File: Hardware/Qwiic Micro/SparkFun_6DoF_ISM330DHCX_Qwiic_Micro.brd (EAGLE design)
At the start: 19.1 x 7.6 mm, 42 parts, among them J1 Qwiic Right Angle, U1 ISM330DHCX

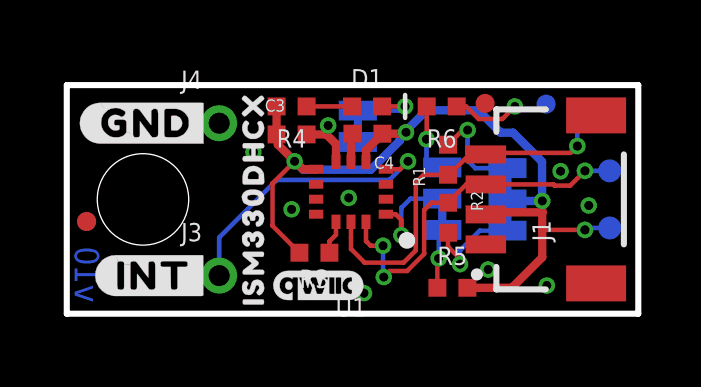
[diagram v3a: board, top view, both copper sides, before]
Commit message: Fixes silk for X-axis, changes tails on INT and GND silk
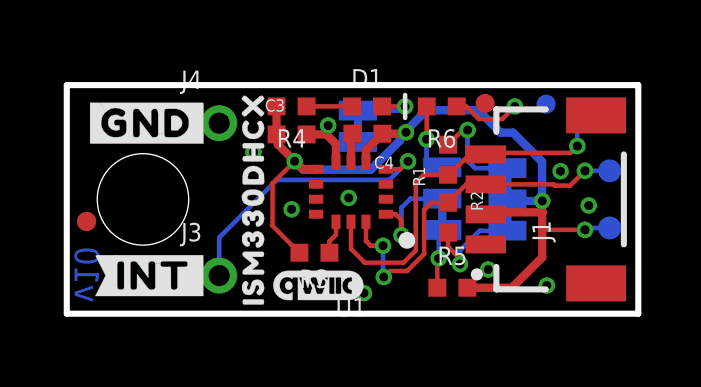
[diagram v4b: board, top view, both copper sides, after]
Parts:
- U$10: device top:#GND#2 -> top:#GND#4
- U$11: device top:#INT#3 -> top:#INT#21
- U$4: device top:#GND#0 -> top:#GND#4
- U$5: device top:#INT#1 -> top:#INT#20
- moved U$7 3.20 mm to (6.10, 1.65)
- moved U$8 3.05 mm to (9.27, 1.57)
- moved U$9 2.72 mm to (8.03, 5.00)
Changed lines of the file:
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@@
 <rectangle x1="9.1948" y1="4.953" x2="9.2456" y2="5.1816" layer="41"/>
 <dimension x1="2.54" y1="3.81" x2="0" y2="3.81" x3="1.27" y3="12.7" textsize="1.778" layer="47" dtype="horizontal" unit="inch"/>
-<wire x1="10.541" y1="3.305175" x2="8.636" y2="3.305175" width="0.254" layer="22"/>
-<wire x1="9.144" y1="2.797175" x2="9.144" y2="3.940175" width="0.254" layer="22" curve="180"/>
-<wire x1="9.144" y1="3.940175" x2="9.398" y2="4.067175" width="0.254" layer="22"/>
-<wire x1="9.144" y1="3.940175" x2="9.271" y2="3.686175" width="0.254" layer="22"/>
-<wire x1="10.541" y1="3.305175" x2="10.287" y2="3.051175" width="0.254" layer="22"/>
-<wire x1="10.541" y1="3.305175" x2="10.287" y2="3.559175" width="0.254" layer="22"/>
-<wire x1="7.635875" y1="0.65405" x2="7.635875" y2="2.43205" width="0.254" layer="22"/>
-<wire x1="7.000875" y1="2.05105" x2="8.270875" y2="2.05105" width="0.254" layer="22" curve="180"/>
-<wire x1="8.270875" y1="2.05105" x2="8.397875" y2="1.79705" width="0.254" layer="22"/>
-<wire x1="8.270875" y1="2.05105" x2="8.042275" y2="1.92405" width="0.254" layer="22"/>
-<wire x1="7.635875" y1="0.65405" x2="7.381875" y2="0.90805" width="0.254" layer="22"/>
-<wire x1="7.635875" y1="0.65405" x2="7.889875" y2="0.90805" width="0.254" layer="22"/>
-<wire x1="7.356475" y1="0.93345" x2="7.915275" y2="0.93345" width="0.254" layer="22"/>
-<wire x1="8.042275" y1="1.92405" x2="8.397875" y2="1.79705" width="0.254" layer="22"/>
-<wire x1="9.398" y1="4.067175" x2="9.271" y2="3.686175" width="0.254" layer="22"/>
-<wire x1="10.287" y1="3.559175" x2="10.287" y2="3.051175" width="0.254" layer="22"/>
-<wire x1="7.38505" y1="4.403725" x2="7.051675" y2="4.45135" width="0.254" layer="22"/>
-<wire x1="7.38505" y1="4.403725" x2="7.25805" y2="4.09575" width="0.254" layer="22"/>
-<wire x1="7.25805" y1="4.09575" x2="7.051675" y2="4.45135" width="0.254" layer="22"/>
-<wire x1="7.254875" y1="4.32435" x2="6.848475" y2="2.71145" width="0.254" layer="22" curve="100"/>
-<circle x="7.7089" y="3.35915" radius="0.5334" width="0.254" layer="22"/>
-<wire x1="8.128" y1="2.921" x2="7.239" y2="3.81" width="0.254" layer="22"/>
-<wire x1="7.366" y1="2.921" x2="8.255" y2="3.81" width="0.254" layer="22"/>
+<wire x1="5.207" y1="3.171825" x2="7.112" y2="3.171825" width="0.254" layer="22"/>
+<wire x1="6.604" y1="3.679825" x2="6.604" y2="2.536825" width="0.254" layer="22" curve="180"/>
+<wire x1="6.604" y1="2.536825" x2="6.35" y2="2.409825" width="0.254" layer="22"/>
+<wire x1="6.604" y1="2.536825" x2="6.477" y2="2.790825" width="0.254" layer="22"/>
+<wire x1="5.207" y1="3.171825" x2="5.461" y2="3.425825" width="0.254" layer="22"/>
+<wire x1="5.207" y1="3.171825" x2="5.461" y2="2.917825" width="0.254" layer="22"/>
+<wire x1="8.016875" y1="0.52705" x2="8.016875" y2="2.30505" width="0.254" layer="22"/>
+<wire x1="7.381875" y1="1.92405" x2="8.651875" y2="1.92405" width="0.254" layer="22" curve="180"/>
+<wire x1="8.651875" y1="1.92405" x2="8.778875" y2="1.67005" width="0.254" layer="22"/>
+<wire x1="8.651875" y1="1.92405" x2="8.423275" y2="1.79705" width="0.254" layer="22"/>
+<wire x1="8.016875" y1="0.52705" x2="7.762875" y2="0.78105" width="0.254" layer="22"/>
+<wire x1="8.016875" y1="0.52705" x2="8.270875" y2="0.78105" width="0.254" layer="22"/>
+<wire x1="7.737475" y1="0.80645" x2="8.296275" y2="0.80645" width="0.254" layer="22"/>
+<wire x1="8.423275" y1="1.79705" x2="8.778875" y2="1.67005" width="0.254" layer="22"/>
+<wire x1="6.35" y1="2.409825" x2="6.477" y2="2.790825" width="0.254" layer="22"/>
+<wire x1="5.461" y1="2.917825" x2="5.461" y2="3.425825" width="0.254" layer="22"/>
+<wire x1="9.229725" y1="3.53695" x2="9.27735" y2="3.870325" width="0.254" layer="22"/>
+<wire x1="9.229725" y1="3.53695" x2="8.92175" y2="3.66395" width="0.254" layer="22"/>
+<wire x1="8.92175" y1="3.66395" x2="9.27735" y2="3.870325" width="0.254" layer="22"/>
+<wire x1="9.15035" y1="3.667125" x2="7.53745" y2="4.073525" width="0.254" layer="22" curve="100"/>
+<circle x="8.0899" y="3.23215" radius="0.5334" width="0.254" layer="22"/>
+<wire x1="8.509" y1="2.794" x2="7.62" y2="3.683" width="0.254" layer="22"/>
+<wire x1="7.747" y1="2.794" x2="8.636" y2="3.683" width="0.254" layer="22"/>
 <dimension x1="19.05" y1="7.62" x2="0" y2="7.62" x3="9.525" y3="16.51" textsize="1.778" textratio="15" layer="47" unit="inch"/>
 <dimension x1="19.05" y1="0" x2="19.05" y2="7.62" x3="27.94" y3="3.81" textsize="1.778" textratio="15" layer="47" unit="inch"/>
@@
 <element name="LOGO1" library="SparkFun-Aesthetics" package="QWIIC_3MM" value="QWIIC_LOGO_3MM" x="8.382" y="0.9398" smashed="yes"/>
 <element name="LOGO3" library="SparkFun-Aesthetics" package="BLANK" value="SFE_LOGO_NAME_FLAMEBLANK" x="-39.37" y="-15.24" smashed="yes"/>
-<element name="U$7" library="ISMTopMini" package="X2114" value="" x="9.271" y="2.032" smashed="yes" rot="MR0"/>
-<element name="U$8" library="ISMTopMini" package="Y2115" value="" x="6.223" y="1.5748" smashed="yes" rot="MR0"/>
-<element name="U$9" library="ISMTopMini" package="Z2116" value="" x="5.8674" y="3.3528" smashed="yes" rot="MR0"/>
+<element name="U$7" library="ISMTopMini" package="X2114" value="" x="6.096" y="1.651" smashed="yes" rot="MR0"/>
+<element name="U$8" library="ISMTopMini" package="Y2115" value="" x="9.271" y="1.5748" smashed="yes" rot="MR0"/>
+<element name="U$9" library="ISMTopMini" package="Z2116" value="" x="8.0264" y="5.0038" smashed="yes" rot="MR0"/>
 <element name="U$3" library="ISMTopMini" package="#LED#2121" value="" x="7.3406" y="6.35" smashed="yes" rot="MR0"/>
 <element name="U$6" library="ISMTopMini" package="ISM330DHCX2120" value="" x="6.223" y="3.8354" smashed="yes" rot="R90"/>
@@
 </element>
 <element name="TP4" library="SparkFun-Connectors" package="PAD.03X.03" value="TEST-POINT3" x="18.0975" y="0.9525" smashed="yes" rot="MR0"/>
-<element name="U$4" library="top" package="#GND#0" value="" x="2.667" y="6.35" smashed="yes"/>
-<element name="U$5" library="top" package="#INT#1" value="" x="2.921" y="1.27" smashed="yes"/>
-<element name="U$10" library="top" package="#GND#2" value="" x="2.667" y="6.35" smashed="yes" rot="MR0"/>
-<element name="U$11" library="top" package="#INT#3" value="" x="2.921" y="1.27" smashed="yes" rot="MR0"/>
 <element name="U$1" library="top" package="#0#4" value="" x="12.573" y="6.35" smashed="yes" rot="MR90"/>
 <element name="U$2" library="top" package="#1#4" value="" x="12.446" y="1.397" smashed="yes" rot="MR90"/>
@@
 <attribute name="VALUE" x="8.255" y="2.594" size="0.6096" layer="27" font="vector" ratio="20" rot="R180" align="top-center"/>
 </element>
+<element name="U$5" library="top" package="#INT#20" value="" x="2.921" y="1.27" smashed="yes"/>
+<element name="U$11" library="top" package="#INT#21" value="" x="2.921" y="1.27" smashed="yes" rot="MR0"/>
+<element name="U$4" library="top" package="#GND#4" value="" x="2.667" y="6.35" smashed="yes"/>
+<element name="U$10" library="top" package="#GND#4" value="" x="2.667" y="6.35" smashed="yes" rot="MR0"/>
 </elements>
 <signals>
